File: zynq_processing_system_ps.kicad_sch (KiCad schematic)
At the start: 0 parts

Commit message: sch_zynq_update
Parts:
- added C404: 100n, Capacitor_SMD:C_0402_1005Metric, symbol Device:C
- added D400: RED, LED_0402_RED, symbol Schematic-Lib-PhilsLab:LED_0402_RED
- added Q400: T2N7002AK, Package_TO_SOT_SMD:SOT-23, symbol Transistor_FET:T2N7002AK
- added R1, R416: 100k, Resistor_SMD:R_0402_1005Metric, symbol Device:R
- added R2, R404: 20K, Resistor_SMD:R_0402_1005Metric, symbol Device:R
- added R406, R407, R408, R409, R410, R411: 22R, Resistor_SMD:R_0402_1005Metric, symbol Device:R
- added R412: 510, Resistor_SMD:R_0402_1005Metric, symbol Device:R
- added R413, R417: 12K, Resistor_SMD:R_0402_1005Metric, symbol Device:R
- added U1: XC7Z020-2CLG400I, Package_BGA:Xilinx_CLG400, symbol 2024-11-30_12-42-37:XC7Z020-2CLG400I
- added U401: SN74LVC1G07DRLR, Footprint-Lib-PhilsLab:SOT-5, symbol Schematic-Lib-PhilsLab:SN74LVC1G07DRLR
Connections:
- new net: D400.K, Q400.3 (D)
- new net +3V3: C404.1, R2.1, R412.2, R417.2, U401.5 (VCC)
- new net ETH_NINT: U1.E12 (PS_MIO42_501)
- new net ETH_NRST: R416.1, U1.C17 (PS_MIO41_501), U401.2 (A)
- new net ETH_NRST_+3V3: R417.1, U401.4 (Y)
- new net ETH_PHY_TXCLK: R406.1
- new net ETH_PHY_TXCTL: R411.1
- new net ETH_PHY_TXD0: R407.1
- new net ETH_PHY_TXD1: R408.1
- new net ETH_PHY_TXD2: R409.1
- new net ETH_PHY_TXD3: R410.1
- new net ETH_RXCLK: U1.B17 (PS_MIO22_501)
- new net ETH_RXCTL: U1.D13 (PS_MIO27_501)
- new net ETH_RXD0: U1.D11 (PS_MIO23_501)
- new net ETH_RXD1: U1.A16 (PS_MIO24_501)
- new net ETH_RXD2: U1.F15 (PS_MIO25_501)
- new net ETH_RXD3: U1.A15 (PS_MIO26_501)
- new net ETH_TXCLK: R406.2, U1.A19 (PS_MIO16_501)
- new net ETH_TXCTL: R411.2, U1.F14 (PS_MIO21_501)
- new net ETH_TXD0: R407.2, U1.E14 (PS_MIO17_501)
- new net ETH_TXD1: R408.2, U1.B18 (PS_MIO18_501)
- new net ETH_TXD2: R409.2, U1.D10 (PS_MIO19_501)
- new net ETH_TXD3: R410.2, U1.A17 (PS_MIO20_501)
- new net FET_PS_G: Q400.1 (G), R413.1
- new net GND: C404.2, Q400.2 (S), R1.2, R404.1, R416.2, U401.3 (GND)
- new net LED_PS_A: D400.A, R412.1
- new net MIO43: U1.A9 (PS_MIO43_501)
- new net MIO44: U1.F13 (PS_MIO44_501)
- new net PS_LED: R1.1, R413.2, U1.E6 (PS_MIO0_500)
- new net QSPI_CLK: U1.A5 (PS_MIO6_500)
- new net QSPI_DQ0_M3: U1.B8 (PS_MIO2_500)
- new net QSPI_DQ1_M1: U1.D6 (PS_MIO3_500)
- new net QSPI_DQ2_M2: U1.B7 (PS_MIO4_500)
- new net QSPI_DQ3_M0: U1.A6 (PS_MIO5_500)
- new net QSPI_NCS: U1.A7 (PS_MIO1_500)
- new net SD_CLK: U1.D9 (PS_MIO12_500)
- new net SD_CMD: U1.C6 (PS_MIO11_500)
- new net SD_D0: U1.E9 (PS_MIO10_500)
- new net SD_D1: U1.E8 (PS_MIO13_500)
- new net SD_D2: U1.C5 (PS_MIO14_500)
- new net SD_D3: U1.C8 (PS_MIO15_500)
- new net UART1_RX: U1.B5 (PS_MIO9_500)
- new net UART1_TX_VCFG1: R2.2, U1.D5 (PS_MIO8_500)
- new net USB_CLK: U1.A11 (PS_MIO36_501)
- new net USB_DATA0: U1.A14 (PS_MIO32_501)
- new net USB_DATA1: U1.D15 (PS_MIO33_501)
- new net USB_DATA2: U1.A12 (PS_MIO34_501)
- new net USB_DATA3: U1.F12 (PS_MIO35_501)
- new net USB_DATA4: U1.C16 (PS_MIO28_501)
- new net USB_DATA5: U1.A10 (PS_MIO37_501)
- new net USB_DATA6: U1.E13 (PS_MIO38_501)
- new net USB_DATA7: U1.C18 (PS_MIO39_501)
- new net USB_DIR: U1.C13 (PS_MIO29_501)
- new net USB_NRST: U1.D14 (PS_MIO40_501)
- new net USB_NXT: U1.E16 (PS_MIO31_501)
- new net USB_STP: U1.C15 (PS_MIO30_501)
- new net VCFG0: R404.2, U1.D8 (PS_MIO7_500)
- no-connect marks 0 -> 1

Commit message: sch_zynq_update
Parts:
- added C405: 100n, Capacitor_SMD:C_0402_1005Metric, symbol Device:C
- added R418: 12K, Resistor_SMD:R_0402_1005Metric, symbol Device:R
- added R419: 22R, Resistor_SMD:R_0402_1005Metric, symbol Device:R
- added U3: S40FC004C1B2I00000, VFBGA153-9.0x7.5x0.8, symbol Schematic-Lib-PhilsLab:S40FC004C1B2I00000
- added U402: W25Q128JVEIQ, Footprint-Lib-PhilsLab:WSON-8-8X6, symbol Schematic-Lib-PhilsLab:W25Q128JVEIQ
- renumbered R2 to R405, R1 to R414
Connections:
- net +3V3: now also C405.1, R418.1, U402.8 (VCC)
- net GND: now also C405.2, U402.4 (GND), U402.9 (EP)
- net QSPI_CLK: now also R419.2
- net QSPI_DQ0_M3: now also U402.5 (DI_IO0)
- net QSPI_DQ1_M1: now also U402.2 (DO_IO1)
- net QSPI_DQ2_M2: now also U402.3 (~{WP}_IO2)
- net QSPI_DQ3_M0: now also U402.7 (~{HOLD}/~{RESET}_IO3)
- net MIO48: now reaches U1.B12 (PS_MIO48_501)
- net MIO50: now reaches U1.B13 (PS_MIO50_501)
- net MIO47: now reaches U1.B14 (PS_MIO47_501)
- net MIO45: now reaches U1.B15 (PS_MIO45_501)
- net MIO51: now reaches U1.B9 (PS_MIO51_501)
- net ETH_MDC: now reaches U1.C10 (PS_MIO52_501)
- net ETH_MDIO: now reaches U1.C11 (PS_MIO53_501)
- net MIO49: now reaches U1.C12 (PS_MIO49_501)
- net MIO46: now reaches U1.D16 (PS_MIO46_501)
- new net: R418.2, U402.1 (~{CS})
- new net FLASH_CLK_M4: R419.1, U402.6 (CLK)

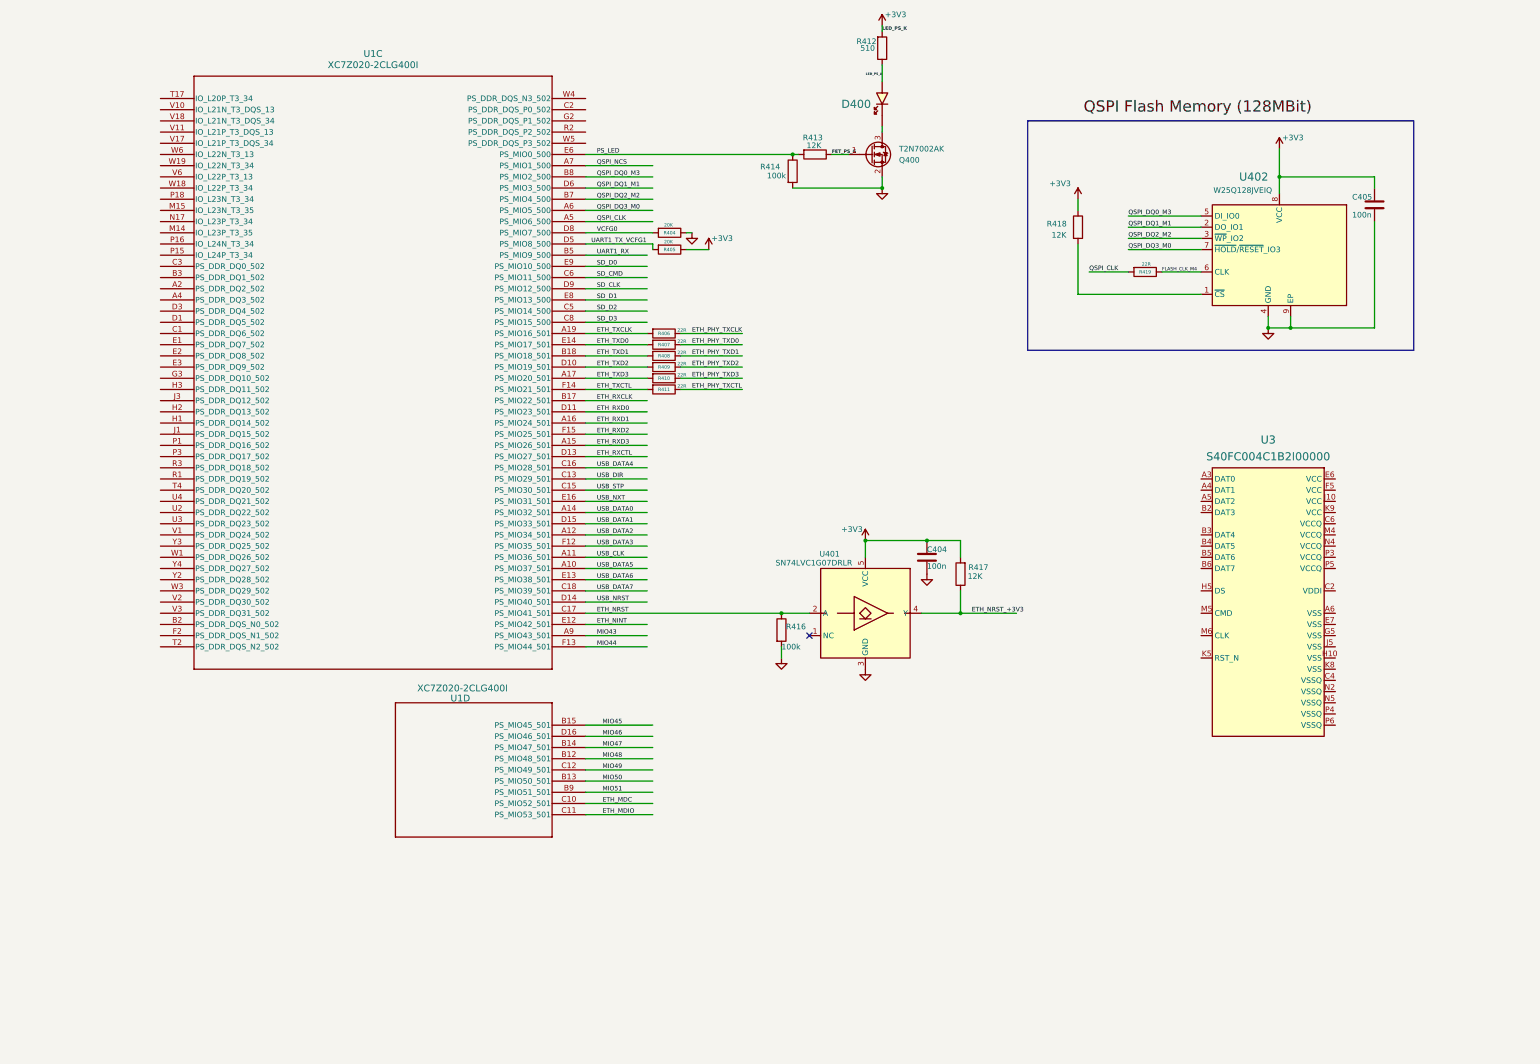
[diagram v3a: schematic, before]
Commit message: sch updated zynq ddr
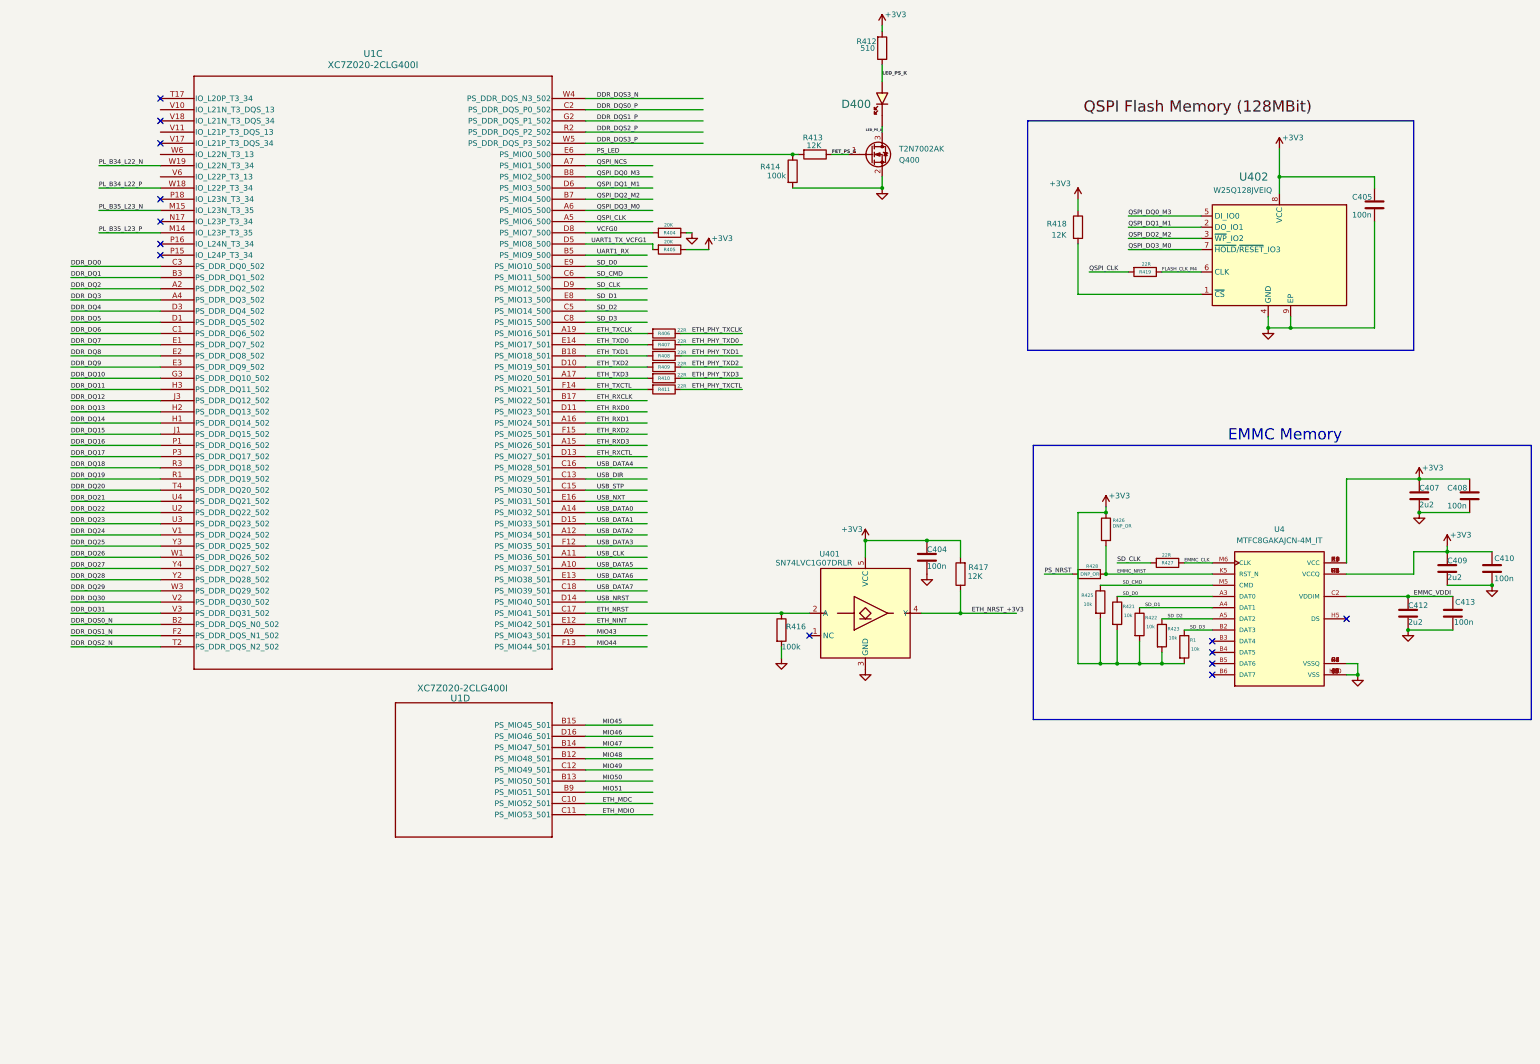
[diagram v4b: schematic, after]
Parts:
- removed U3: S40FC004C1B2I00000, VFBGA153-9.0x7.5x0.8, symbol Schematic-Lib-PhilsLab:S40FC004C1B2I00000
- added C407, C409, C412: 2u2, Capacitor_SMD:C_0402_1005Metric, symbol Device:C
- added C408, C410, C413: 100n, Capacitor_SMD:C_0402_1005Metric, symbol Device:C
- added R1, R421, R422, R423, R425: 10k, Resistor_SMD:R_0402_1005Metric, symbol Device:R
- added R426, R428: DNP_OR, Resistor_SMD:R_0402_1005Metric, symbol Device:R
- added R427: 22R, Resistor_SMD:R_0402_1005Metric, symbol Device:R
- added U4: MTFC8GAKAJCN-4M_IT, MTFC8GAKAJCN-4M_IT:BGA153N50P14X14_1150X1300X100, symbol MTFC8GAKAJCN-4M IT:MTFC8GAKAJCN-4M_IT
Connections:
- net +3V3: now also C407.1, C408.1, C409.1, C410.1, R1.2, R421.2, R422.2, R423.2, R425.2, R426.1, U4.C6 (VCCQ), U4.E6 (VCC), U4.F5 (VCC), U4.J10 (VCC), U4.K9 (VCC), U4.M4 (VCCQ), U4.N4 (VCCQ), U4.P3 (VCCQ), U4.P5 (VCCQ)
- net GND: now also C407.2, C408.2, C409.2, C410.2, C412.2, C413.2, U4.A6 (VSS), U4.C4 (VSSQ), U4.E7 (VSS), U4.G5 (VSS), U4.H10 (VSS), U4.J5 (VSS), U4.K8 (VSS), U4.N2 (VSSQ), U4.N5 (VSSQ), U4.P4 (VSSQ), U4.P6 (VSSQ)
- net LED_PS_A: now also D400.K, Q400.3 (D); no longer D400.A, R412.1
- net SD_CLK: now also R427.2
- net SD_CMD: now also R425.1, U4.M5 (CMD)
- net SD_D0: now also R421.1, U4.A3 (DAT0)
- net SD_D1: now also R422.1, U4.A4 (DAT1)
- net SD_D2: now also R423.1, U4.A5 (DAT2)
- net SD_D3: now also R1.1, U4.B2 (DAT3)
- net DDR_DQ2: now reaches U1.A2 (PS_DDR_DQ2_502)
- net DDR_DQ3: now reaches U1.A4 (PS_DDR_DQ3_502)
- net DDR_DQS0_N: now reaches U1.B2 (PS_DDR_DQS_N0_502)
- net DDR_DQ1: now reaches U1.B3 (PS_DDR_DQ1_502)
- net DDR_DQ6: now reaches U1.C1 (PS_DDR_DQ6_502)
- net DDR_DQS0_P: now reaches U1.C2 (PS_DDR_DQS_P0_502)
- net DDR_DQ0: now reaches U1.C3 (PS_DDR_DQ0_502)
- net DDR_DQ5: now reaches U1.D1 (PS_DDR_DQ5_502)
- net DDR_DQ4: now reaches U1.D3 (PS_DDR_DQ4_502)
- net DDR_DQ7: now reaches U1.E1 (PS_DDR_DQ7_502)
- net DDR_DQ8: now reaches U1.E2 (PS_DDR_DQ8_502)
- net DDR_DQ9: now reaches U1.E3 (PS_DDR_DQ9_502)
- net DDR_DQS1_N: now reaches U1.F2 (PS_DDR_DQS_N1_502)
- net DDR_DQS1_P: now reaches U1.G2 (PS_DDR_DQS_P1_502)
- net DDR_DQ10: now reaches U1.G3 (PS_DDR_DQ10_502)
- net DDR_DQ14: now reaches U1.H1 (PS_DDR_DQ14_502)
- net DDR_DQ13: now reaches U1.H2 (PS_DDR_DQ13_502)
- net DDR_DQ11: now reaches U1.H3 (PS_DDR_DQ11_502)
- net DDR_DQ15: now reaches U1.J1 (PS_DDR_DQ15_502)
- net DDR_DQ12: now reaches U1.J3 (PS_DDR_DQ12_502)
- net PL_B35_L23_P: now reaches U1.M14 (IO_L23P_T3_35)
- net PL_B35_L23_N: now reaches U1.M15 (IO_L23N_T3_35)
- net DDR_DQ16: now reaches U1.P1 (PS_DDR_DQ16_502)
- net DDR_DQ17: now reaches U1.P3 (PS_DDR_DQ17_502)
- net DDR_DQ19: now reaches U1.R1 (PS_DDR_DQ19_502)
- net DDR_DQS2_P: now reaches U1.R2 (PS_DDR_DQS_P2_502)
- net DDR_DQ18: now reaches U1.R3 (PS_DDR_DQ18_502)
- net DDR_DQS2_N: now reaches U1.T2 (PS_DDR_DQS_N2_502)
- net DDR_DQ20: now reaches U1.T4 (PS_DDR_DQ20_502)
- net DDR_DQ22: now reaches U1.U2 (PS_DDR_DQ22_502)
- net DDR_DQ23: now reaches U1.U3 (PS_DDR_DQ23_502)
- net DDR_DQ21: now reaches U1.U4 (PS_DDR_DQ21_502)
- net DDR_DQ24: now reaches U1.V1 (PS_DDR_DQ24_502)
- net DDR_DQ30: now reaches U1.V2 (PS_DDR_DQ30_502)
- net DDR_DQ31: now reaches U1.V3 (PS_DDR_DQ31_502)
- net DDR_DQ26: now reaches U1.W1 (PS_DDR_DQ26_502)
- net PL_B34_L22_P: now reaches U1.W18 (IO_L22P_T3_34)
- net PL_B34_L22_N: now reaches U1.W19 (IO_L22N_T3_34)
- net DDR_DQ29: now reaches U1.W3 (PS_DDR_DQ29_502)
- net DDR_DQS3_N: now reaches U1.W4 (PS_DDR_DQS_N3_502)
- net DDR_DQS3_P: now reaches U1.W5 (PS_DDR_DQS_P3_502)
- net DDR_DQ28: now reaches U1.Y2 (PS_DDR_DQ28_502)
- net DDR_DQ25: now reaches U1.Y3 (PS_DDR_DQ25_502)
- net DDR_DQ27: now reaches U1.Y4 (PS_DDR_DQ27_502)
- new net EMMC_CLK: R427.1, U4.M6 (CLK)
- new net EMMC_NRST: R426.2, R428.2, U4.K5 (RST_N)
- new net EMMC_VDDI: C412.1, C413.1, U4.C2 (VDDIM)
- new net LED_PS_K: D400.A, R412.1
- new net PS_NRST: R428.1
- no-connect marks 1 -> 13
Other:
- note added: "EMMC Memory"

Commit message: all page
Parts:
- removed U1: XC7Z020-2CLG400I, Package_BGA:Xilinx_CLG400, symbol 2024-11-30_12-42-37:XC7Z020-2CLG400I
- added C400, C401, C402, C403, C406: 100n, Capacitor_SMD:C_0402_1005Metric, symbol Device:C
- added R400, R401, R402: 12K, Resistor_SMD:R_0402_1005Metric, symbol Device:R
- added R403: 4K7, Resistor_SMD:R_0402_1005Metric, symbol Device:R
- added R420: 22R, Resistor_SMD:R_0402_1005Metric, symbol Device:R
- added SW400: SKRPANE010, SKRPANE010, symbol Schematic-Lib-PhilsLab:SKRPANE010
- added U400: SN74LVC1G07DRLR, Footprint-Lib-PhilsLab:SOT-5, symbol Schematic-Lib-PhilsLab:SN74LVC1G07DRLR
- added U6: XC7Z020-2CLG400I, zynq_sc7z0x0:CLG400, symbol Zynq_xc7z0x0-x:CMP-0363-00007-3
- added X1: ECS-2520MV-33.3, XTAL_2520, symbol Schematic-Lib-PhilsLab:ECS-2520MV-130-BN-TR
- renumbered R1 to R424
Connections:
- net +3V3: now also C403.1, C406.1, R403.1, U400.5 (VCC), X1.1 (EN), X1.4 (VDD)
- net ETH_MDC: now also U6.C10 (PS_MIO52_501)
- net ETH_MDIO: now also U6.C11 (PS_MIO53_501)
- net ETH_NINT: now also U6.E12 (PS_MIO42_501)
- net ETH_NRST: now also U6.C17 (PS_MIO41_501)
- net ETH_RXCLK: now also U6.B17 (PS_MIO22_501)
- net ETH_RXCTL: now also U6.D13 (PS_MIO27_501)
- net ETH_RXD0: now also U6.D11 (PS_MIO23_501)
- net ETH_RXD1: now also U6.A16 (PS_MIO24_501)
- net ETH_RXD2: now also U6.F15 (PS_MIO25_501)
- net ETH_RXD3: now also U6.A15 (PS_MIO26_501)
- net ETH_TXCLK: now also U6.A19 (PS_MIO16_501)
- net ETH_TXCTL: now also U6.F14 (PS_MIO21_501)
- net ETH_TXD0: now also U6.E14 (PS_MIO17_501)
- net ETH_TXD1: now also U6.B18 (PS_MIO18_501)
- net ETH_TXD2: now also U6.D10 (PS_MIO19_501)
- net ETH_TXD3: now also U6.A17 (PS_MIO20_501)
- net GND: now also C400.1, C402.2, C403.2, C406.2, R401.2, U400.3 (GND), X1.2 (GND)
- net MIO43: now also U6.A9 (PS_MIO43_501)
- net MIO44: now also U6.F13 (PS_MIO44_501)
- net MIO45: now also U6.B15 (PS_MIO45_501)
- net MIO46: now also U6.D16 (PS_MIO46_501)
- net MIO47: now also U6.B14 (PS_MIO47_501)
- net MIO48: now also U6.B12 (PS_MIO48_501)
- net MIO49: now also U6.C12 (PS_MIO49_501)
- net MIO50: now also U6.B13 (PS_MIO50_501)
- net MIO51: now also U6.B9 (PS_MIO51_501)
- net PS_LED: now also U6.E6 (PS_MIO0_500)
- net PS_NRST: now also C401.1, R402.1, SW400.12, U6.B10 (PS_SRST_B_501)
- net QSPI_CLK: now also U6.A5 (PS_MIO6_500)
- net QSPI_DQ0_M3: now also U6.B8 (PS_MIO2_500)
- net QSPI_DQ1_M1: now also U6.D6 (PS_MIO3_500)
- net QSPI_DQ2_M2: now also U6.B7 (PS_MIO4_500)
- net QSPI_DQ3_M0: now also U6.A6 (PS_MIO5_500)
- net QSPI_NCS: now also U6.A7 (PS_MIO1_500)
- net SD_CLK: now also U6.D9 (PS_MIO12_500)
- net SD_CMD: now also U6.C6 (PS_MIO11_500)
- net SD_D0: now also U6.E9 (PS_MIO10_500)
- net SD_D1: now also U6.E8 (PS_MIO13_500)
- net SD_D2: now also U6.C5 (PS_MIO14_500)
- net SD_D3: now also U6.C8 (PS_MIO15_500)
- net UART1_RX: now also U6.B5 (PS_MIO9_500)
- net UART1_TX_VCFG1: now also U6.D5 (PS_MIO8_500)
- net USB_CLK: now also U6.A11 (PS_MIO36_501)
- net USB_DATA0: now also U6.A14 (PS_MIO32_501)
- net USB_DATA1: now also U6.D15 (PS_MIO33_501)
- net USB_DATA2: now also U6.A12 (PS_MIO34_501)
- net USB_DATA3: now also U6.F12 (PS_MIO35_501)
- net USB_DATA4: now also U6.C16 (PS_MIO28_501)
- net USB_DATA5: now also U6.A10 (PS_MIO37_501)
- net USB_DATA6: now also U6.E13 (PS_MIO38_501)
- net USB_DATA7: now also U6.C18 (PS_MIO39_501)
- net USB_DIR: now also U6.C13 (PS_MIO29_501)
- net USB_NRST: now also U6.D14 (PS_MIO40_501)
- net USB_NXT: now also U6.E16 (PS_MIO31_501)
- net USB_STP: now also U6.C15 (PS_MIO30_501)
- net VCFG0: now also U6.D8 (PS_MIO7_500)
- new net: C401.2, SW400.34
- new net +1V8: R400.1, R402.2
- new net CLK_33M33: R420.2, X1.3 (OUT)
- new net MIO_VRFF_OV9: C400.2, R400.2, R401.1, U6.E11 (PS_MIO_VREF_501)
- new net PG_3V3: U400.2 (A)
- new net PS_CLK_33M333: R420.1, U6.E7 (PS_CLK_500)
- new net PS_NPOR: C402.1, R403.2, U400.4 (Y), U6.C7 (PS_POR_B_500)
- no-connect marks 13 -> 7
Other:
- note added: "PS Clock (33.33 MHz)"
- note added: "PS_NPOR"
- note added: "PS_NRST"
- note added: "QSPI Flash Memory (128MBit)"
- note added: "Zynq PS (Bank 500 & 501)"
- moved on the sheet: C404, D400, Q400, R404, R405, R406, R407, R408, R409, R410, R411, R412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

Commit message: sch-to-pcb
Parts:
- renumbered U4 to U403, X1 to X400
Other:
- moved on the sheet: R405, R413, R414, R418

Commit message: xc7z020-fanout
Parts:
- U6: footprint zynq_sc7z0x0:CLG400 -> Package_BGA:Xilinx_CLG400
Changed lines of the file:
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@@
 			)
 		)
-		(property "Footprint" "zynq_sc7z0x0:CLG400"
+		(property "Footprint" "Package_BGA:Xilinx_CLG400"
 			(at 63.5 90.17 0)
 			(effects
